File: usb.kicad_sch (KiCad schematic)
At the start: 21 parts, among them J13 USB-C_TYPE-C_16PLT-H6.5, J7 USB-A_USB-303WSD-BRY, U1 AP22615AWU-7

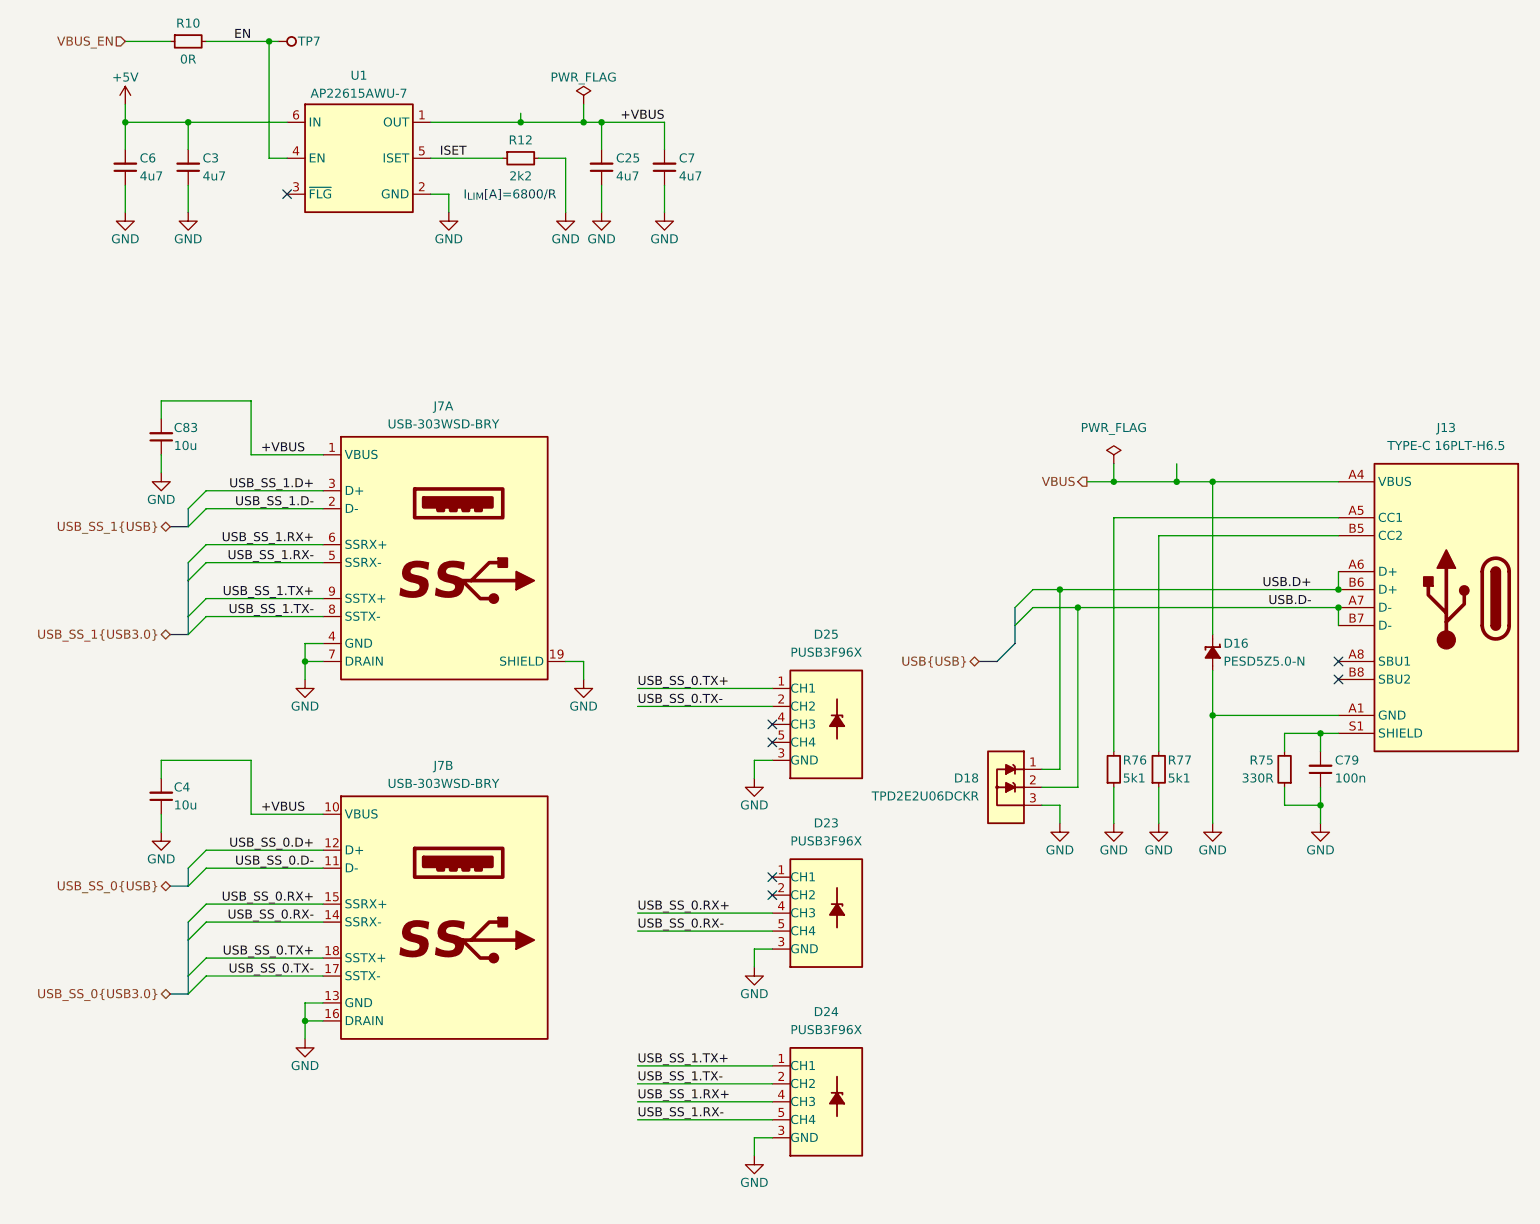
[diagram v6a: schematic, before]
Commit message: [#3] WIP: Clear ERC, re-annotate schematic
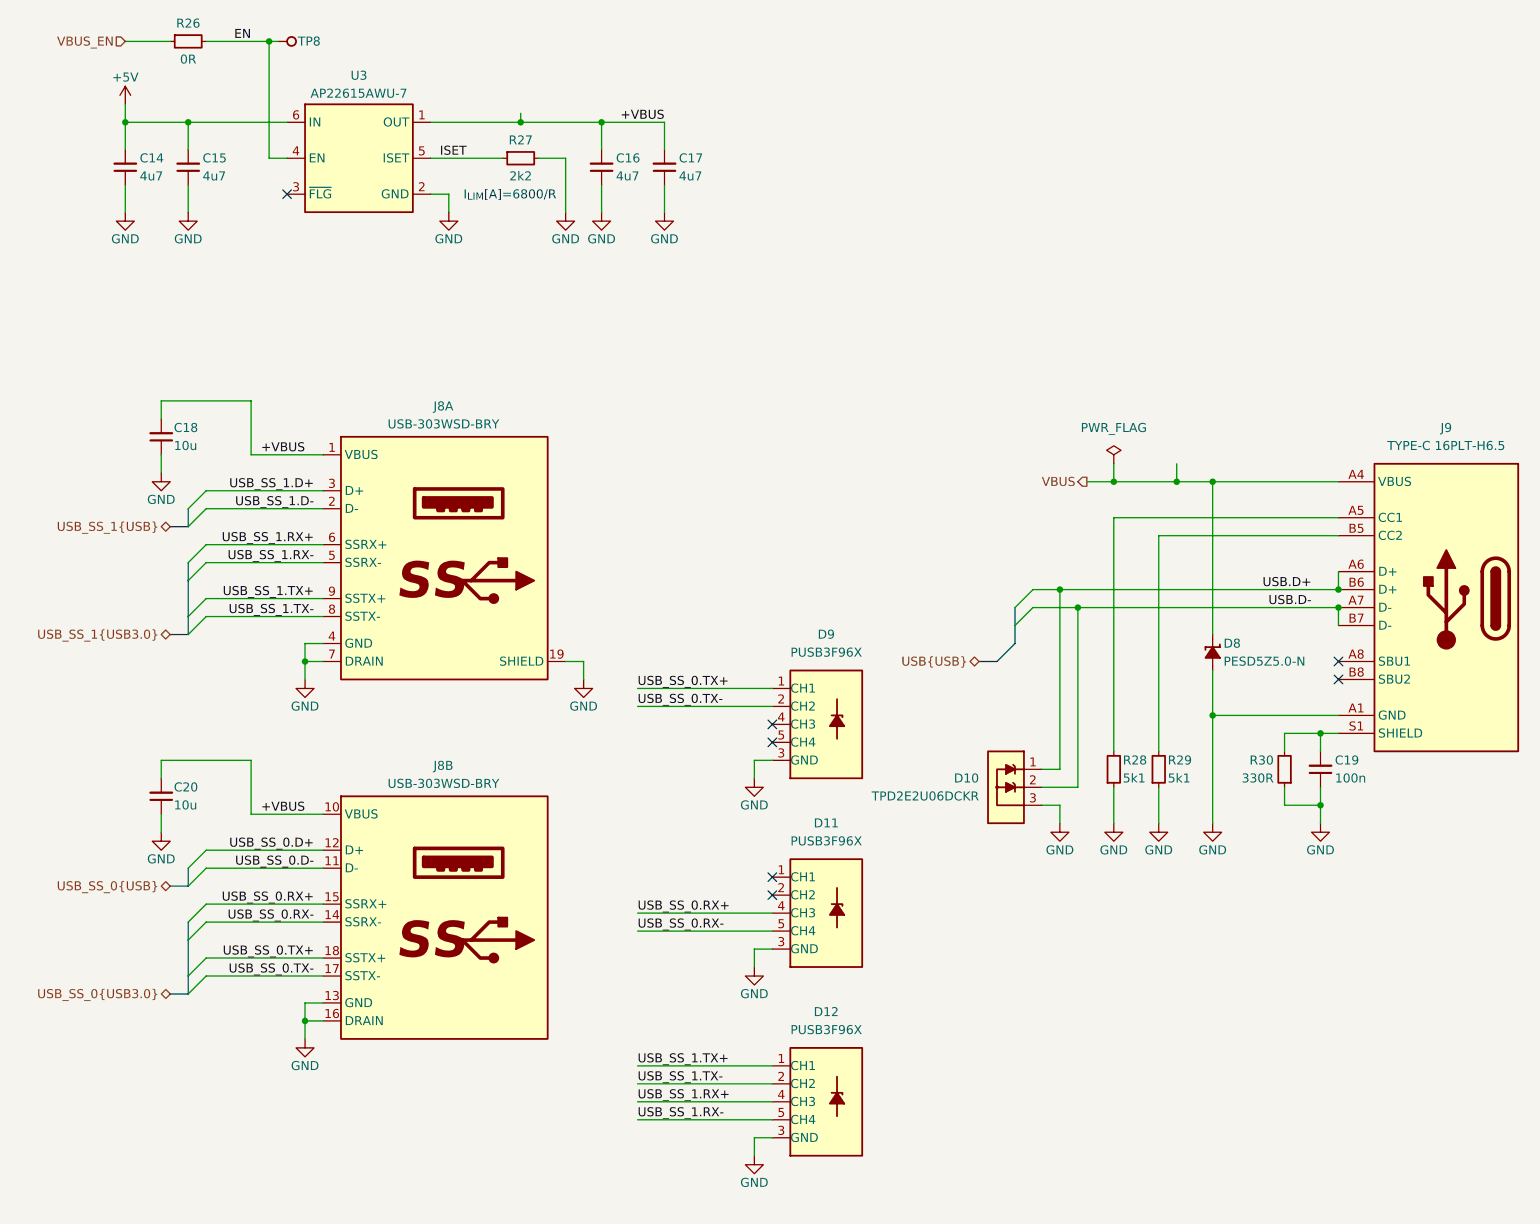
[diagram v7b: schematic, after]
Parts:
- renumbered C6 to C14, C3 to C15, C25 to C16, C7 to C17, C83 to C18, C79 to C19, C4 to C20, D18 to D10, D23 to D11, D24 to D12, D16 to D8, D25 to D9, J7 to J8, J13 to J9, R10 to R26, R12 to R27, R76 to R28, R77 to R29, R75 to R30, TP7 to TP8, U1 to U3

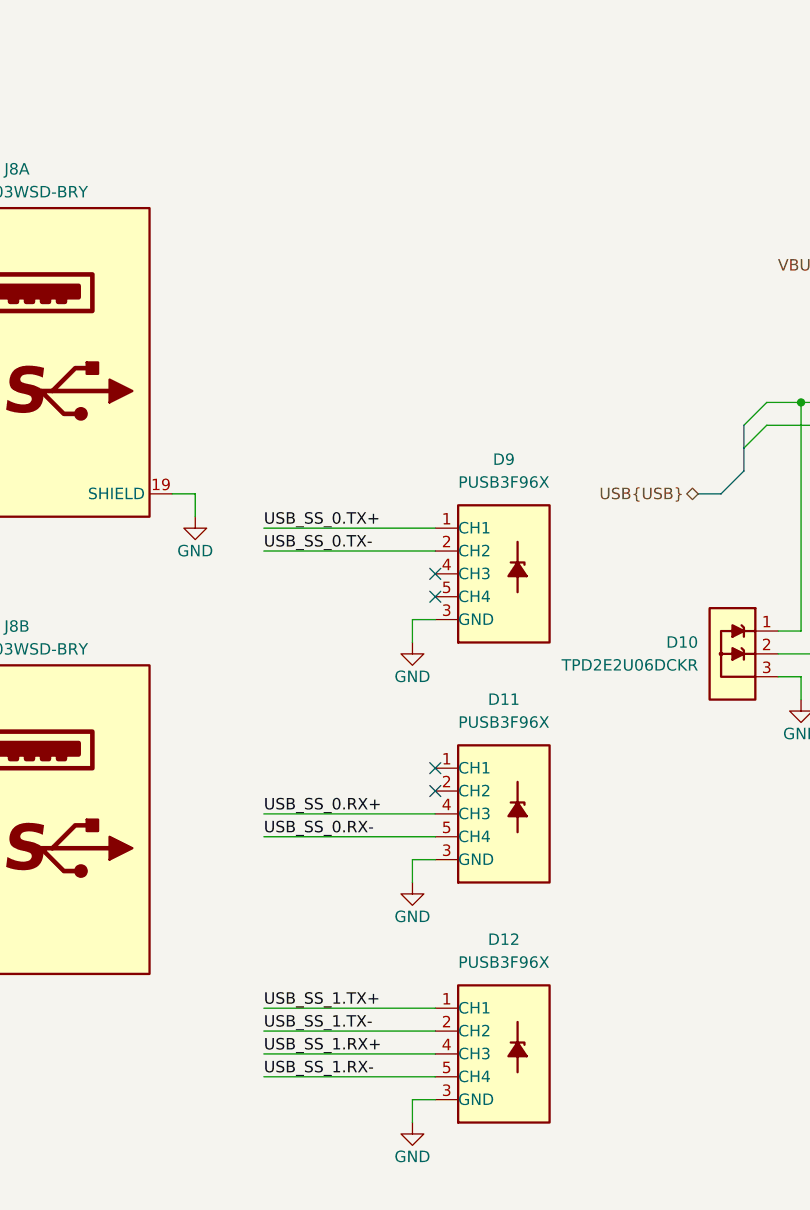
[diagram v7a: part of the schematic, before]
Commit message: [#3] Layout USB
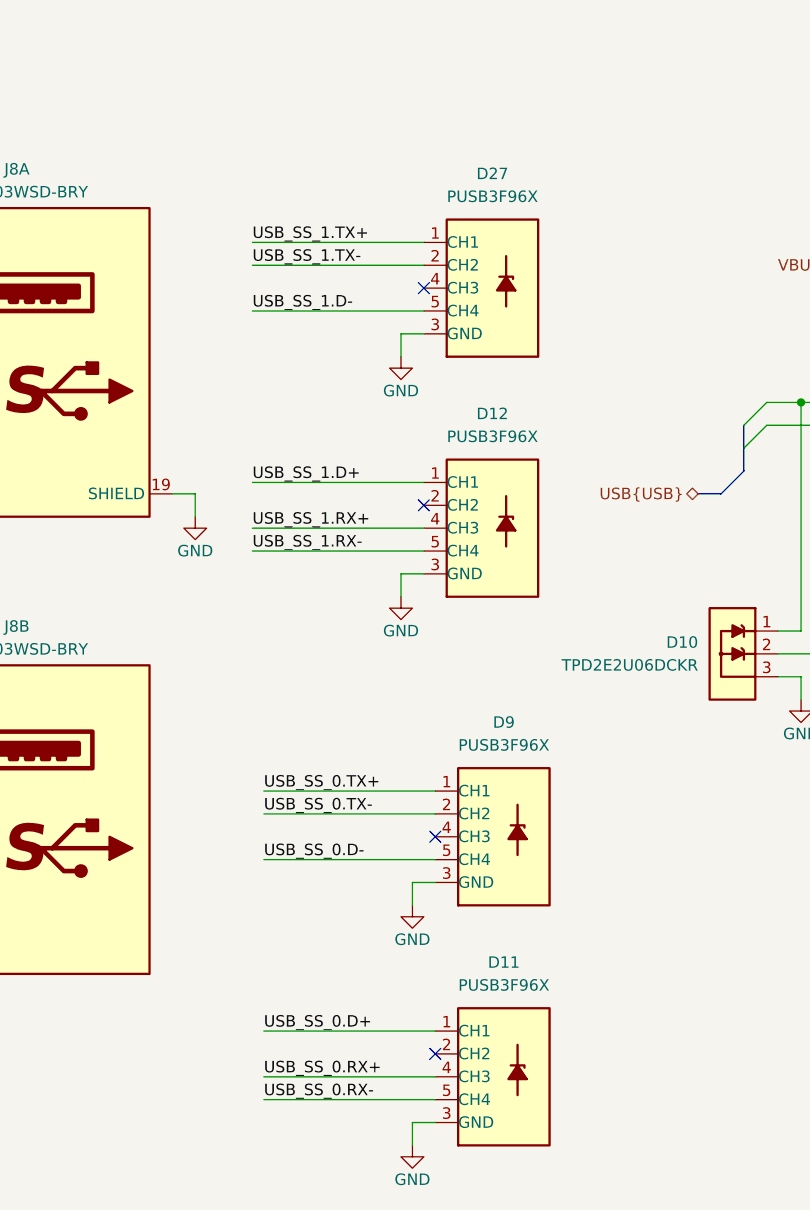
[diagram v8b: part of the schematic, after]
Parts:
- added D27: PUSB3F96X, DW-footprints:SOT1176-1, symbol DW-TVS:PUSB3F96X
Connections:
- net GND: now also D27.3 (GND), D27.8 (GND)
- net USB_SS_0.D+: now also D11.1 (CH1), D11.10 (CH1)
- net USB_SS_0.D-: now also D9.5 (CH4), D9.6 (CH4)
- net USB_SS_1.D+: now also D12.1 (CH1), D12.10 (CH1)
- net USB_SS_1.D-: now also D27.5 (CH4), D27.6 (CH4)
- net USB_SS_1.TX+: now also D27.1 (CH1), D27.10 (CH1); no longer D12.1 (CH1), D12.10 (CH1)
- net USB_SS_1.TX-: now also D27.2 (CH2), D27.9 (CH2); no longer D12.2 (CH2), D12.9 (CH2)
- new net: D27.4 (CH3), D27.7 (CH3)
- new net: D12.2 (CH2), D12.9 (CH2)
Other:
- moved on the sheet: D11, D12, D9
